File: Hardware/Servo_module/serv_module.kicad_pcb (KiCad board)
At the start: 2 copper layers, 56 parts, among them K1 CONN_3, K2 CONN_3, K3 CONN_3, K4 CONN_3, K5 CONN_3, K6 CONN_3, K7 CONN_3, K8 CONN_3, P1 CONN_4_JST, P2 CONN_2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

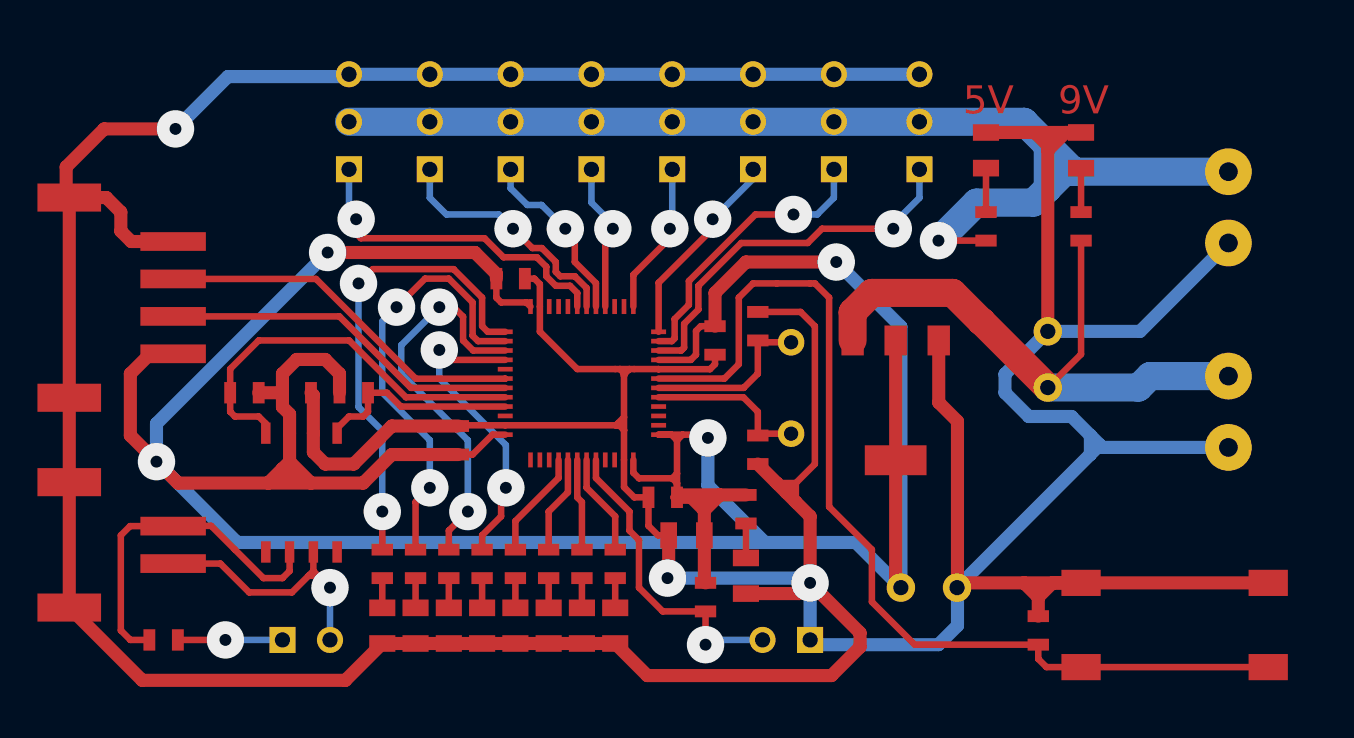
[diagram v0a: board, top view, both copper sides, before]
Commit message: [HARDWARE][SERVO_MODULE] Board legend
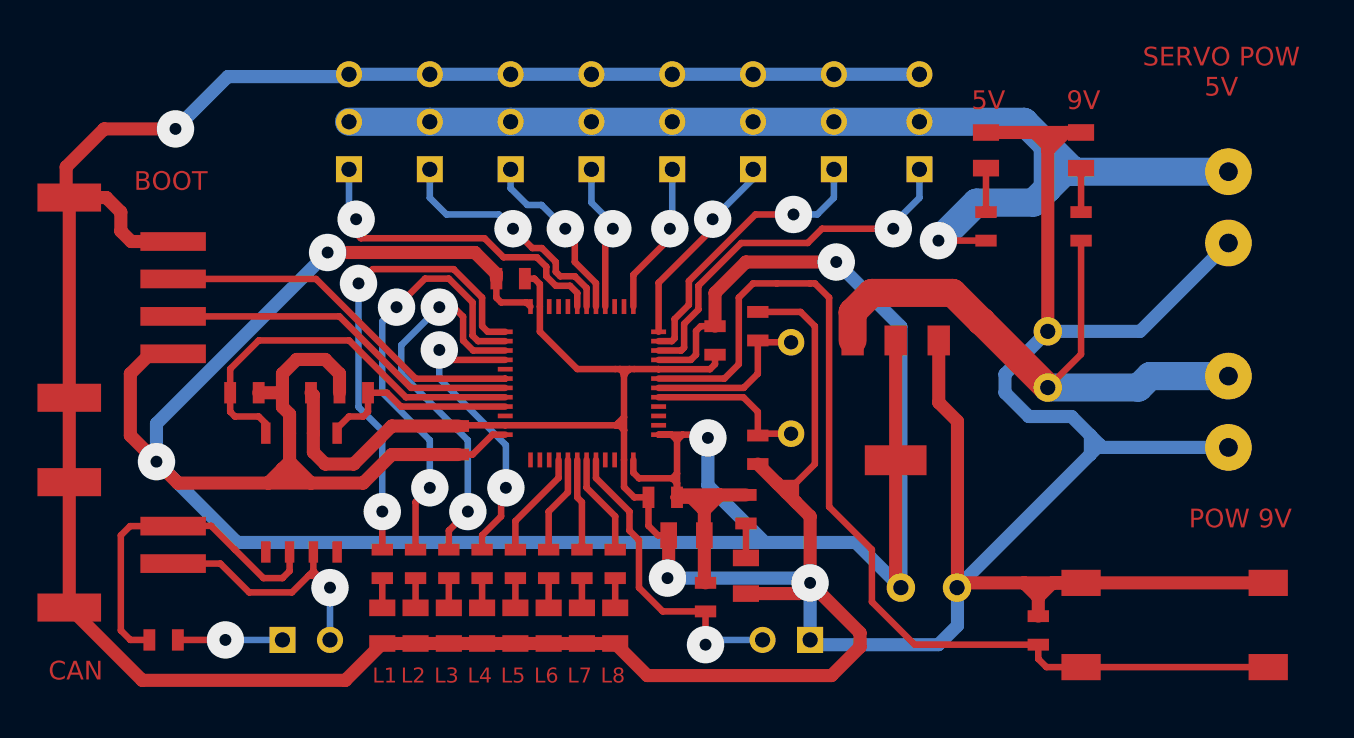
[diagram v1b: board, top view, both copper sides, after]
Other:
- board text added: "BOOT"
- board text added: "CAN"
- board text added: "L1"
- board text added: "L2"
- board text added: "L3"
- board text added: "L4"
- board text added: "L5"
- board text added: "L6"
- board text added: "L7"
- board text added: "L8"
- board text added: "POW 9V"
- board text added: "SERVO POW 5V"
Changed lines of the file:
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@@
     (links 123)
     (no_connects 0)
-    (area 0 0 0 0)
+    (area 154.560001 97.231999 236.9566 138.336)
     (thickness 1.6)
-    (drawings 2)
+    (drawings 21)
     (tracks 499)
     (zones 0)
@@
     (pad_to_mask_clearance 0)
     (aux_axis_origin 0 0)
-    (visible_elements 7FFFFFFF)
+    (visible_elements 7FFF7FFF)
     (pcbplotparams
       (layerselection 3178497)
@@
   (module CP_D4_S15 (layer Dessus.Cu)
     (at 213.741 127.381)
-    (fp_text reference CP2 (at -7.00024 5.99948) (layer Dessus.SilkS)
+    (fp_text reference CP2 (at 0.127 5.207) (layer Dessus.SilkS)
       (effects (font (size 1.524 1.524) (thickness 0.3048)))
     )
@@
   (module CP_D4_S15 (layer Dessus.Cu)
     (at 220.091 115.189 90)
-    (fp_text reference CP1 (at -7.00024 5.99948 90) (layer Dessus.SilkS)
+    (fp_text reference CP1 (at -5.461 0.127 180) (layer Dessus.SilkS)
       (effects (font (size 1.524 1.524) (thickness 0.3048)))
     )
@@
     )
   )
+  (gr_line (start 165.1 97.282) (end 165.1 133.604) (angle 90) (layer Contours.Ci) (width 0.1))
+  (gr_line (start 233.934 97.282) (end 165.1 97.282) (angle 90) (layer Contours.Ci) (width 0.1))
+  (dimension 36.322 (width 0.3) (layer Contours.Ci)
+    (gr_text "36,322 mm" (at 161.21 115.443 90) (layer Contours.Ci)
+      (effects (font (size 1.5 1.5) (thickness 0.3)))
+    )
+    (feature1 (pts (xy 165.1 97.282) (xy 159.86 97.282)))
+    (feature2 (pts (xy 165.1 133.604) (xy 159.86 133.604)))
+    (crossbar (pts (xy 162.56 133.604) (xy 162.56 97.282)))
+    (arrow1a (pts (xy 162.56 97.282) (xy 163.14642 98.408503)))
+    (arrow1b (pts (xy 162.56 97.282) (xy 161.97358 98.408503)))
+    (arrow2a (pts (xy 162.56 133.604) (xy 163.14642 132.477497)))
+    (arrow2b (pts (xy 162.56 133.604) (xy 161.97358 132.477497)))
+  )
+  (dimension 68.834 (width 0.3) (layer Contours.Ci)
+    (gr_text "68,834 mm" (at 199.517 136.985999) (layer Contours.Ci)
+      (effects (font (size 1.5 1.5) (thickness 0.3)))
+    )
+    (feature1 (pts (xy 233.934 133.604) (xy 233.934 138.335999)))
+    (feature2 (pts (xy 165.1 133.604) (xy 165.1 138.335999)))
+    (crossbar (pts (xy 165.1 135.635999) (xy 233.934 135.635999)))
+    (arrow1a (pts (xy 233.934 135.635999) (xy 232.807497 136.222419)))
+    (arrow1b (pts (xy 233.934 135.635999) (xy 232.807497 135.049579)))
+    (arrow2a (pts (xy 165.1 135.635999) (xy 166.226503 136.222419)))
+    (arrow2b (pts (xy 165.1 135.635999) (xy 166.226503 135.049579)))
+  )
+  (gr_line (start 233.934 133.604) (end 165.1 133.604) (angle 90) (layer Contours.Ci) (width 0.1))
+  (gr_text BOOT (at 173.228 105.664) (layer Dessus.Cu)
+    (effects (font (size 1 1) (thickness 0.25)))
+  )
+  (gr_text CAN (at 168.148 131.826) (layer Dessus.Cu)
+    (effects (font (size 1 1) (thickness 0.25)))
+  )
+  (gr_text "POW 9V" (at 230.378 123.698) (layer Dessus.Cu)
+    (effects (font (size 1 1) (thickness 0.25)))
+  )
+  (gr_text "SERVO POW\n5V" (at 229.362 99.822) (layer Dessus.Cu)
+    (effects (font (size 1 1) (thickness 0.25)))
+  )
+  (gr_text L8 (at 196.85 132.08) (layer Dessus.Cu)
+    (effects (font (size 0.8 0.8) (thickness 0.2)))
+  )
+  (gr_text L7 (at 195.072 132.08) (layer Dessus.Cu)
+    (effects (font (size 0.8 0.8) (thickness 0.2)))
+  )
+  (gr_text L6 (at 193.294 132.08) (layer Dessus.Cu)
+    (effects (font (size 0.8 0.8) (thickness 0.2)))
+  )
+  (gr_text L5 (at 191.516 132.08) (layer Dessus.Cu)
+    (effects (font (size 0.8 0.8) (thickness 0.2)))
+  )
+  (gr_text L4 (at 189.738 132.08) (layer Dessus.Cu)
+    (effects (font (size 0.8 0.8) (thickness 0.2)))
+  )
+  (gr_text L3 (at 187.96 132.08) (layer Dessus.Cu)
+    (effects (font (size 0.8 0.8) (thickness 0.2)))
+  )
+  (gr_text L2 (at 186.182 132.08) (layer Dessus.Cu)
+    (effects (font (size 0.8 0.8) (thickness 0.2)))
+  )
+  (gr_text L1 (at 184.658 132.08) (layer Dessus.Cu)
+    (effects (font (size 0.8 0.8) (thickness 0.2)))
+  )
+  (gr_line (start 233.934 97.282) (end 233.934 98.552) (angle 90) (layer Contours.Ci) (width 0.1))
+  (gr_line (start 233.934 98.044) (end 233.934 133.604) (angle 90) (layer Contours.Ci) (width 0.1))
   (gr_text 5V (at 216.916 101.346) (layer Dessus.Cu)
-    (effects (font (size 1.5 1.5) (thickness 0.3)))
-  )
-  (gr_text 9V (at 221.996 101.346 360) (layer Dessus.Cu)
-    (effects (font (size 1.5 1.5) (thickness 0.3)))
+    (effects (font (size 1 1) (thickness 0.25)))
+  )
+  (gr_text 9V (at 221.996 101.346) (layer Dessus.Cu)
+    (effects (font (size 1 1) (thickness 0.25)))
   )
   (segment (start 172.466 120.65) (end 172.466 118.618) (width 0.70104) (layer Dessous.Cu) (net 1))
@@
   (segment (start 208.026 108.204) (end 211.836 108.204) (width 0.35052) (layer Dessus.Cu) (net 8))
   (via (at 211.836 108.204) (size 1.99898) (layers Dessus.Cu Dessous.Cu) (net 8))
-  (segment (start 199.29602 114.71148) (end 200.50252 114.71148) (width 0.35052) (layer Dessus.Cu) (net 8) (status 400000))
-  (segment (start 213.233 106.553) (end 213.233 105.029) (width 0.35052) (layer Dessous.Cu) (net 8) (status 800000))
+  (segment (start 199.29602 114.71148) (end 200.50252 114.71148) (width 0.35052) (layer Dessus.Cu) (net 8))
+  (segment (start 213.233 106.553) (end 213.233 105.029) (width 0.35052) (layer Dessous.Cu) (net 8))
   (segment (start 211.836 107.95) (end 213.233 106.553) (width 0.35052) (layer Dessous.Cu) (net 8))
   (segment (start 206.502 107.442) (end 207.772 107.442) (width 0.35052) (layer Dessous.Cu) (net 9))
@@
   (segment (start 204.47 107.442) (end 206.502 107.442) (width 0.35052) (layer Dessus.Cu) (net 9))
   (via (at 206.502 107.442) (size 1.99898) (layers Dessus.Cu Dessous.Cu) (net 9))
-  (segment (start 199.29602 114.2111) (end 200.004678 114.2111) (width 0.35052) (layer Dessus.Cu) (net 9) (status 400000))
-  (segment (start 208.661 106.553) (end 208.661 105.029) (width 0.35052) (layer Dessous.Cu) (net 9) (status 800000))
+  (segment (start 199.29602 114.2111) (end 200.004678 114.2111) (width 0.35052) (layer Dessus.Cu) (net 9))
+  (segment (start 208.661 106.553) (end 208.661 105.029) (width 0.35052) (layer Dessous.Cu) (net 9))
   (segment (start 207.772 107.442) (end 208.661 106.553) (width 0.35052) (layer Dessous.Cu) (net 9))
-  (segment (start 199.29602 113.71072) (end 199.29602 111.09198) (width 0.35052) (layer Dessus.Cu) (net 10) (status 400000))
-  (segment (start 204.343 105.537) (end 204.343 105.029) (width 0.35052) (layer Dessous.Cu) (net 10) (status C00000))
-  (segment (start 202.184 107.696) (end 204.343 105.537) (width 0.35052) (layer Dessous.Cu) (net 10) (status 800000))
+  (segment (start 199.29602 113.71072) (end 199.29602 111.09198) (width 0.35052) (layer Dessus.Cu) (net 10))
+  (segment (start 204.343 105.537) (end 204.343 105.029) (width 0.35052) (layer Dessous.Cu) (net 10))
+  (segment (start 202.184 107.696) (end 204.343 105.537) (width 0.35052) (layer Dessous.Cu) (net 10))
   (via (at 202.184 107.696) (size 1.99898) (layers Dessus.Cu Dessous.Cu) (net 10))
   (segment (start 202.184 108.204) (end 202.184 107.696) (width 0.35052) (layer Dessus.Cu) (net 10))
@@
   (segment (start 186.321698 116.217698) (end 191.10198 116.217698) (width 0.35052) (layer Dessus.Cu) (net 18))
   (segment (start 180.99024 110.88624) (end 186.321698 116.217698) (width 0.35052) (layer Dessus.Cu) (net 18))
-  (segment (start 167.8051 128.44526) (end 167.81526 128.44526) (width 0.70104) (layer Dessus.Cu) (net 19) (status C00000))
-  (segment (start 182.5625 132.334) (end 184.531 130.3655) (width 0.70104) (layer Dessus.Cu) (net 19) (status 800000))
+  (segment (start 167.8051 128.44526) (end 167.81526 128.44526) (width 0.70104) (layer Dessus.Cu) (net 19))
+  (segment (start 182.5625 132.334) (end 184.531 130.3655) (width 0.70104) (layer Dessus.Cu) (net 19))
   (segment (start 171.704 132.334) (end 182.5625 132.334) (width 0.70104) (layer Dessus.Cu) (net 19))
-  (segment (start 167.81526 128.44526) (end 171.704 132.334) (width 0.70104) (layer Dessus.Cu) (net 19) (status 400000))
+  (segment (start 167.81526 128.44526) (end 171.704 132.334) (width 0.70104) (layer Dessus.Cu) (net 19))
   (segment (start 197.104 118.618) (end 197.0151 118.7069) (width 0.35052) (layer Dessus.Cu) (net 19))
   (segment (start 197.0151 118.7069) (end 197.104 118.7069) (width 0.35052) (layer Dessus.Cu) (net 19))

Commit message: [HARDWARE][SERVO_MOTEUR] Schematic and routing fixes
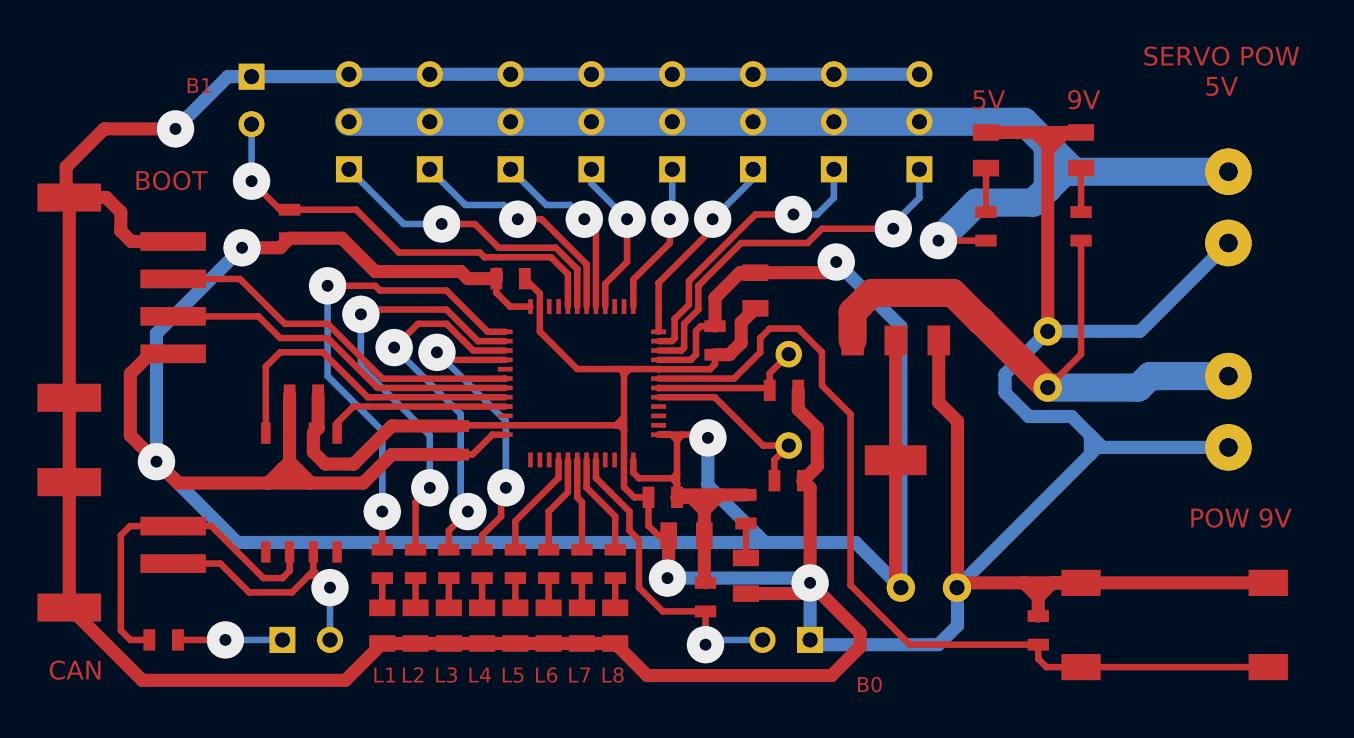
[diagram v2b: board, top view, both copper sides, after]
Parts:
- removed R15: 100k, SM0603_Resistor
- added C10: 1u, SM0805, F.Cu at (204.5, 111.5)
- added JP3: JUMPER, SIL-2, F.Cu at (177.5, 101.3)
- C1: value 100n -> 10n
- moved R14 9.33 mm to (179.6, 108.0), turned to 90 degrees
- moved C8 3.70 mm to (206.0, 116.8), turned to 0 degrees
- moved C7 2.33 mm to (206.2, 121.7), turned to 0 degrees
- moved X1 0.65 mm to (206.2, 117.3)
- moved C9 0.40 mm to (180.3, 117.1)
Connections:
- R14 pad 2: /microcontroller/CAN_RX -> /microcontroller/BOOT1
- U1 pad 20: (no net) -> /microcontroller/BOOT1
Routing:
- net /microcontroller/BOOT1: track 0.00 -> 23.7 mm, vias 0 -> 1
- net GND: track 320.3 -> 312.5 mm
- net /microcontroller/NRST: track 53.9 -> 48.5 mm
- net +3.3V: track 187.8 -> 183.8 mm
- net /microcontroller/CAN_RX: track 21.5 -> 17.7 mm
- net /microcontroller/OSC_IN: track 8.71 -> 10.2 mm
- net /microcontroller/PWM8: track 17.7 -> 16.4 mm
- net /microcontroller/CAN_TX: track 10.9 -> 9.90 mm
- net N-0000028: track 20.9 -> 20.0 mm
- net /microcontroller/OSC_OUT: track 9.21 -> 8.36 mm
- net /microcontroller/PWM5: track 7.97 -> 8.60 mm
- net N-0000033: track 25.2 -> 25.8 mm
- net N-0000030: track 23.5 -> 22.9 mm
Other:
- board text added: "B0"
- board text added: "B1"
